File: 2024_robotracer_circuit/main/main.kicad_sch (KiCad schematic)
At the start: 70 parts, among them J1 PH_6p, J10 PH_5p, J11 PH_6p, J12 PH_4p, J13 PH_8p, J14 PH_6p, J2 Conn_02x05_Odd_Even, J3 Conn_02x05_Odd_Even, J4 PA_2p, J5 PA_2p, J6 XT_2p, J7 HX_12p, J8 PH_4p, J9 PH_5p, SW1 TVGP01-G73BB, U1 STM32F405RGTx, U10 MTN2306AN3, U16 AE-BMX055, U17 MTN2306AN3, U2 SIT2001B, U22 SKRHAAE010, U23 SS-22F32G5, U3 AM2837, U4 AM2837, U5 BP5293-33, U6 BP5293-50, U7 SSM6J808R, U8 MTN2306AN3

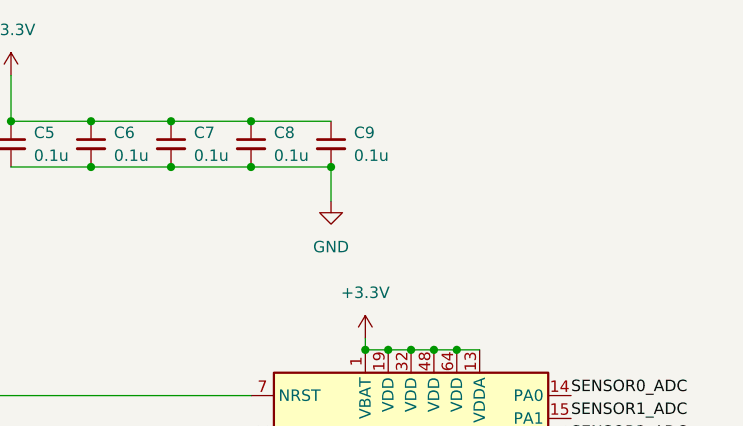
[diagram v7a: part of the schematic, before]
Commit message: マイコン回転させる前
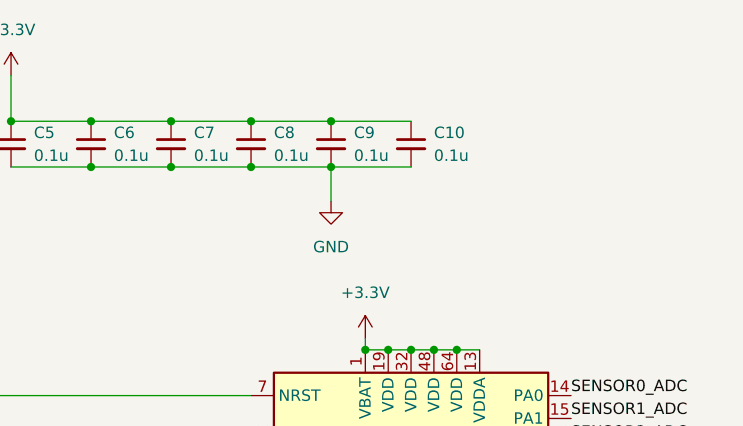
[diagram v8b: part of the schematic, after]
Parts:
- added C10: 0.1u, Capacitor_SMD:C_0603_1608Metric_Pad1.08x0.95mm_HandSolder, symbol Device:C_Small
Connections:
- net +3.3V: now also C10.1
- net GND: now also C10.2
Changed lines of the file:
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@@
 	)
 	(junction
+		(at 325.12 34.29)
+		(diameter 0)
+		(color 0 0 0 0)
+	)
+	(junction
 		(at 78.74 163.83)
 		(diameter 0)
@@
 	(wire
 		(pts
+			(xy 325.12 34.29) (xy 334.01 34.29)
+		)
+		(stroke
+			(width 0)
+			(type default)
+		)
+	)
+	(wire
+		(pts
 			(xy 193.04 219.71) (xy 193.04 222.25)
 		)
@@
 	(wire
 		(pts
+			(xy 325.12 39.37) (xy 334.01 39.37)
+		)
+		(stroke
+			(width 0)
+			(type default)
+		)
+	)
+	(wire
+		(pts
 			(xy 246.38 74.93) (xy 246.38 80.01)
 		)
@@
 					(unit 1)
 				)
+			)
+		)
+	)
+	(symbol
+		(lib_id "Device:C_Small")
+		(at 334.01 36.83 0)
+		(unit 1)
+		(exclude_from_sim no)
+		(in_bom yes)
+		(on_board yes)
+		(dnp no)
+		(property "Reference" "C10"
+			(at 336.55 35.5662 0)
+			(effects
+				(font
+					(size 1.27 1.27)
+				)
+				(justify left)
+			)
+		)
+		(property "Value" "0.1u"
+			(at 336.55 38.1062 0)
+			(effects
+				(font
+					(size 1.27 1.27)
+				)
+				(justify left)
+			)
+		)
+		(property "Footprint" "Capacitor_SMD:C_0603_1608Metric_Pad1.08x0.95mm_HandSolder"
+			(at 334.01 36.83 0)
+			(effects
+				(font
+					(size 1.27 1.27)
+				)
+				(hide yes)
+			)
+		)
+		(property "Datasheet" "~"
+			(at 334.01 36.83 0)
+			(effects
+				(font
+					(size 1.27 1.27)
+				)
+				(hide yes)
+			)
+		)
+		(property "Description" "Unpolarized capacitor, small symbol"
+			(at 334.01 36.83 0)
+			(effects
+				(font
+					(size 1.27 1.27)
+				)
+				(hide yes)
+			)
+		)
+		(pin "1"
+		)
+		(pin "2"
+		)
+		(instances
+			(project "main"
+				(path "/17779a84-a458-4dfa-8c72-c0044fe3feb5"
+					(reference "C10")
+					(unit 1)
+				)
